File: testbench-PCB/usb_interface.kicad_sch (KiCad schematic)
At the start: 14 parts, among them J1 USB_C_Receptacle_USB2.0, U10 CH340C, U9 USBLC6-2SC6

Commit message: Routing the PCB.
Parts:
- added D1: LED, LED_SMD:LED_0805_2012Metric, symbol Device:LED
- added R4: 500R, Resistor_SMD:R_0805_2012Metric, symbol Device:R
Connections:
- net +5V: now also D1.2 (A)
- net GND: now also R4.2
- new net: D1.1 (K), R4.1
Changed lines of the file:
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@@
+    (stroke (width 0) (type default))
+  )
+  (wire (pts (xy 262.89 118.11) (xy 262.89 121.92))
     (stroke (width 0) (type default))
   )
@@
     (stroke (width 0) (type default))
   )
+  (wire (pts (xy 262.89 105.41) (xy 262.89 110.49))
+    (stroke (width 0) (type default))
+  )
   (wire (pts (xy 218.44 50.8) (xy 218.44 63.5))
     (stroke (width 0) (type default))
@@
   )
   (bus (pts (xy 254 66.04) (xy 254 52.07))
+    (stroke (width 0) (type default))
+  )
+  (wire (pts (xy 262.89 93.98) (xy 262.89 97.79))
     (stroke (width 0) (type default))
   )
@@
         (path "/3ac6901d-218d-4b34-8c4a-bf7c417c33bc/85a3a829-d3a3-466d-ad77-bb3f90e9de82"
           (reference "#PWR06") (unit 1)
+        )
+      )
+    )
+  )
+  (symbol (lib_id "power:GND") (at 262.89 121.92 0) (unit 1)
+    (in_bom yes) (on_board yes) (dnp no) (fields_autoplaced)
+    (property "Reference" "#PWR049" (at 262.89 128.27 0)
+      (effects (font (size 1.27 1.27)) hide)
+    )
+    (property "Value" "GND" (at 262.89 127 0)
+      (effects (font (size 1.27 1.27)))
+    )
+    (property "Footprint" "" (at 262.89 121.92 0)
+      (effects (font (size 1.27 1.27)) hide)
+    )
+    (property "Datasheet" "" (at 262.89 121.92 0)
+      (effects (font (size 1.27 1.27)) hide)
+    )
+    (pin "1")
+    (instances
+      (project "testbench"
+        (path "/3ac6901d-218d-4b34-8c4a-bf7c417c33bc/85a3a829-d3a3-466d-ad77-bb3f90e9de82"
+          (reference "#PWR049") (unit 1)
         )
       )
@@
     )
   )
+  (symbol (lib_id "power:+5V") (at 262.89 93.98 0) (unit 1)
+    (in_bom yes) (on_board yes) (dnp no) (fields_autoplaced)
+    (property "Reference" "#PWR048" (at 262.89 97.79 0)
+      (effects (font (size 1.27 1.27)) hide)
+    )
+    (property "Value" "+5V" (at 262.89 88.9 0)
+      (effects (font (size 1.27 1.27)))
+    )
+    (property "Footprint" "" (at 262.89 93.98 0)
+      (effects (font (size 1.27 1.27)) hide)
+    )
+    (property "Datasheet" "" (at 262.89 93.98 0)
+      (effects (font (size 1.27 1.27)) hide)
+    )
+    (pin "1")
+    (instances
+      (project "testbench"
+        (path "/3ac6901d-218d-4b34-8c4a-bf7c417c33bc/85a3a829-d3a3-466d-ad77-bb3f90e9de82"
+          (reference "#PWR048") (unit 1)
+        )
+      )
+    )
+  )
   (symbol (lib_id "power:GND") (at 111.76 68.58 0) (unit 1)
     (in_bom yes) (on_board yes) (dnp no) (fields_autoplaced)
@@
         (path "/3ac6901d-218d-4b34-8c4a-bf7c417c33bc/85a3a829-d3a3-466d-ad77-bb3f90e9de82"
           (reference "#FLG02") (unit 1)
+        )
+      )
+    )
+  )
+  (symbol (lib_id "Device:R") (at 262.89 114.3 0) (unit 1)
+    (in_bom yes) (on_board yes) (dnp no)
+    (property "Reference" "R4" (at 267.97 114.3 90)
+      (effects (font (size 1.27 1.27)))
+    )
+    (property "Value" "500R" (at 265.43 114.3 90)
+      (effects (font (size 1.27 1.27)))
+    )
+    (property "Footprint" "Resistor_SMD:R_0805_2012Metric" (at 261.112 114.3 90)
+      (effects (font (size 1.27 1.27)) hide)
+    )
+    (property "Datasheet" "~" (at 262.89 114.3 0)
+      (effects (font (size 1.27 1.27)) hide)
+    )
+    (pin "1")
+    (pin "2")
+    (instances
+      (project "testbench"
+        (path "/3ac6901d-218d-4b34-8c4a-bf7c417c33bc"
+          (reference "R4") (unit 1)
+        )
+        (path "/3ac6901d-218d-4b34-8c4a-bf7c417c33bc/08a6730c-9a7c-47f6-b930-4f7799d77218"
+          (reference "R15") (unit 1)
+        )
+        (path "/3ac6901d-218d-4b34-8c4a-bf7c417c33bc/85a3a829-d3a3-466d-ad77-bb3f90e9de82"
+          (reference "R15") (unit 1)
         )
       )
@@
         )
       )
+    )
+  )
+  (symbol (lib_id "Device:LED") (at 262.89 101.6 90) (unit 1)
+    (in_bom yes) (on_board yes) (dnp no)
+    (property "Reference" "D1" (at 259.08 102.87 0)
+      (effects (font (size 1.27 1.27)))
+    )
+    (property "Value" "LED" (at 259.08 103.1875 0)
+      (effects (font (size 1.27 1.27)) hide)
+    )
+    (property "Footprint" "LED_SMD:LED_0805_2012Metric" (at 262.89 101.6 0)
+      (effects (font (size 1.27 1.27)) hide)
+    )
+    (property "Datasheet" "~" (at 262.89 101.6 0)
+      (effects (font (size 1.27 1.27)) hide)
+    )
+    (pin "1")
+    (pin "2")
+    (instances
+      (project "testbench"
+        (path "/3ac6901d-218d-4b34-8c4a-bf7c417c33bc/08a6730c-9a7c-47f6-b930-4f7799d77218"
+          (reference "D1") (unit 1)
+        )
+        (path "/3ac6901d-218d-4b34-8c4a-bf7c417c33bc/85a3a829-d3a3-466d-ad77-bb3f90e9de82"
+          (reference "D1") (unit 1)
+        )
+      )

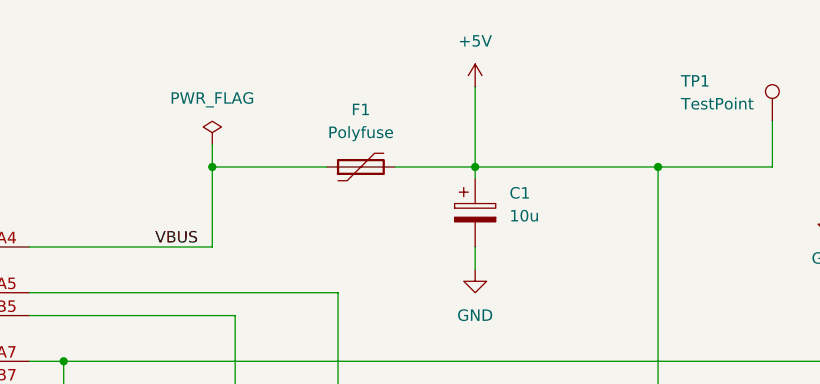
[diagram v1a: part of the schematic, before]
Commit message: Finished PCB routing, added ground plane.
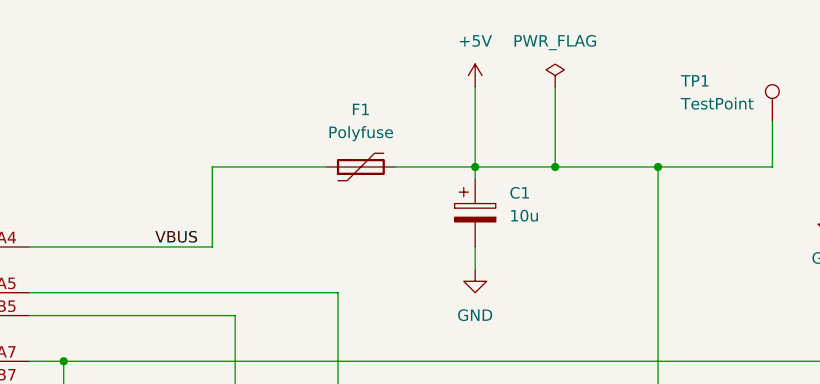
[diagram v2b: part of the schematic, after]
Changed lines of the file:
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@@
   (junction (at 189.23 63.5) (diameter 0) (color 0 0 0 0)
   )
-  (junction (at 82.55 57.15) (diameter 0) (color 0 0 0 0)
-  )
   (junction (at 111.76 57.15) (diameter 0) (color 0 0 0 0)
+  )
+  (junction (at 120.65 57.15) (diameter 0) (color 0 0 0 0)
   )
   (junction (at 66.04 86.36) (diameter 0) (color 0 0 0 0)
@@
     (stroke (width 0) (type default))
   )
-  (wire (pts (xy 82.55 54.61) (xy 82.55 57.15))
-    (stroke (width 0) (type default))
-  )
   (wire (pts (xy 62.23 81.28) (xy 66.04 81.28))
     (stroke (width 0) (type default))
@@
     (stroke (width 0) (type default))
   )
+  (wire (pts (xy 120.65 48.26) (xy 120.65 57.15))
+    (stroke (width 0) (type default))
+  )
   (wire (pts (xy 121.92 106.68) (xy 116.84 106.68))
     (stroke (width 0) (type default))
@@
     (stroke (width 0) (type default))
   )
-  (wire (pts (xy 111.76 57.15) (xy 132.08 57.15))
+  (wire (pts (xy 111.76 57.15) (xy 120.65 57.15))
     (stroke (width 0) (type default))
   )
@@
   )
   (wire (pts (xy 215.9 53.34) (xy 215.9 63.5))
+    (stroke (width 0) (type default))
+  )
+  (wire (pts (xy 120.65 57.15) (xy 132.08 57.15))
     (stroke (width 0) (type default))
   )
@@
         (path "/3ac6901d-218d-4b34-8c4a-bf7c417c33bc/85a3a829-d3a3-466d-ad77-bb3f90e9de82"
           (reference "#PWR05") (unit 1)
+        )
+      )
+    )
+  )
+  (symbol (lib_id "power:PWR_FLAG") (at 120.65 48.26 0) (unit 1)
+    (in_bom yes) (on_board yes) (dnp no) (fields_autoplaced)
+    (property "Reference" "#FLG01" (at 120.65 46.355 0)
+      (effects (font (size 1.27 1.27)) hide)
+    )
+    (property "Value" "PWR_FLAG" (at 120.65 43.18 0)
+      (effects (font (size 1.27 1.27)))
+    )
+    (property "Footprint" "" (at 120.65 48.26 0)
+      (effects (font (size 1.27 1.27)) hide)
+    )
+    (property "Datasheet" "~" (at 120.65 48.26 0)
+      (effects (font (size 1.27 1.27)) hide)
+    )
+    (pin "1")
+    (instances
+      (project "testbench"
+        (path "/3ac6901d-218d-4b34-8c4a-bf7c417c33bc/85a3a829-d3a3-466d-ad77-bb3f90e9de82"
+          (reference "#FLG01") (unit 1)
         )
       )
@@
         )
       )
-    )
-  )
-  (symbol (lib_id "power:PWR_FLAG") (at 82.55 54.61 0) (unit 1)
-    (in_bom yes) (on_board yes) (dnp no) (fields_autoplaced)
-    (property "Reference" "#FLG01" (at 82.55 52.705 0)
-      (effects (font (size 1.27 1.27)) hide)
-    )
-    (property "Value" "PWR_FLAG" (at 82.55 49.53 0)
-      (effects (font (size 1.27 1.27)))
-    )
-    (property "Footprint" "" (at 82.55 54.61 0)
-      (effects (font (size 1.27 1.27)) hide)
-    )
-    (property "Datasheet" "~" (at 82.55 54.61 0)
-      (effects (font (size 1.27 1.27)) hide)
-    )
-    (pin "1")
-    (instances
-      (project "testbench"
-        (path "/3ac6901d-218d-4b34-8c4a-bf7c417c33bc/85a3a829-d3a3-466d-ad77-bb3f90e9de82"
-          (reference "#FLG01") (unit 1)
-        )
-      )

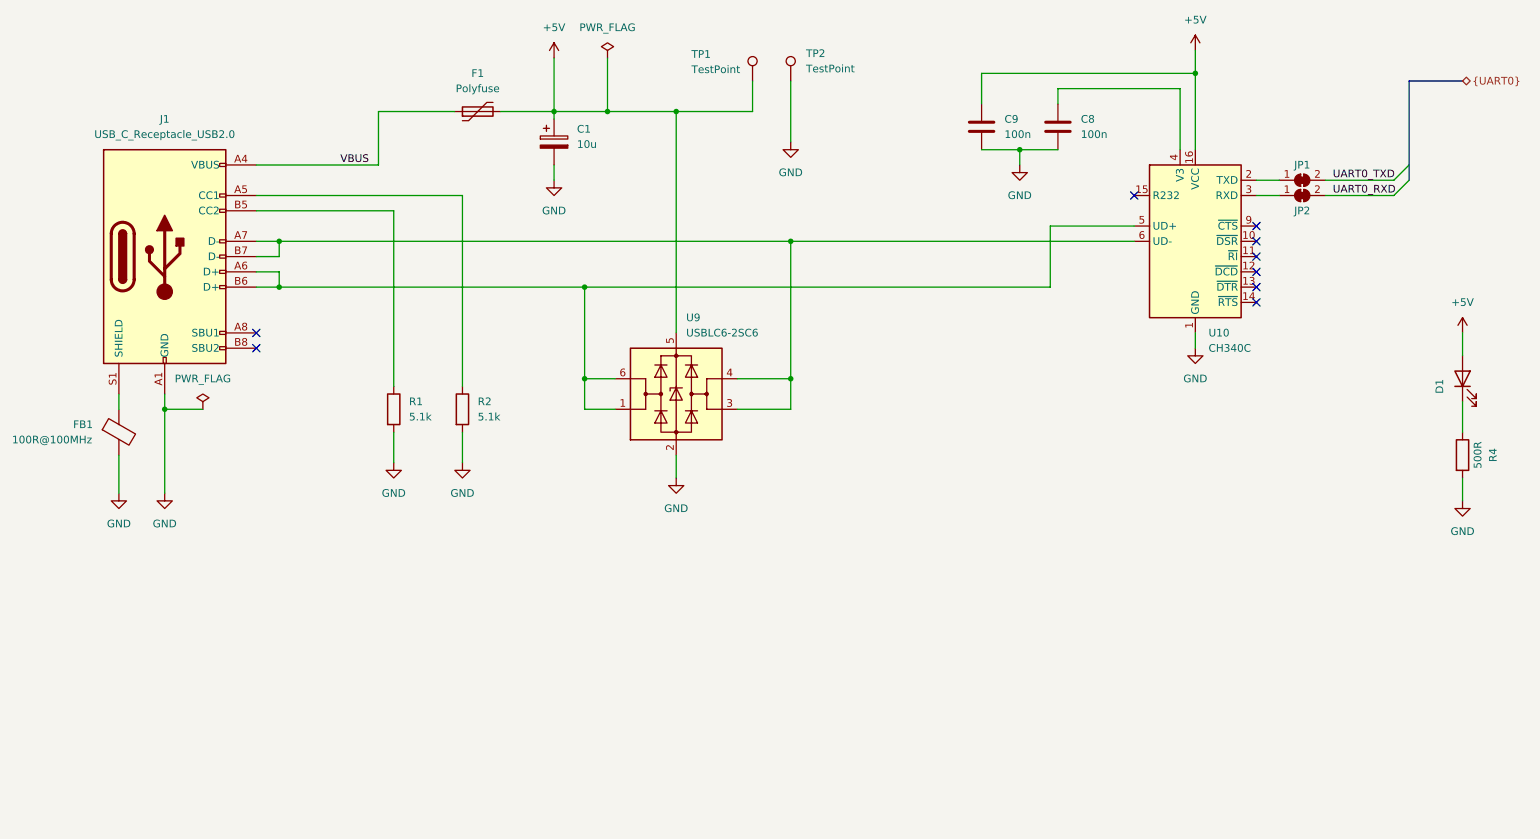
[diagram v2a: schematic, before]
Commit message: Changes regarding part selection.
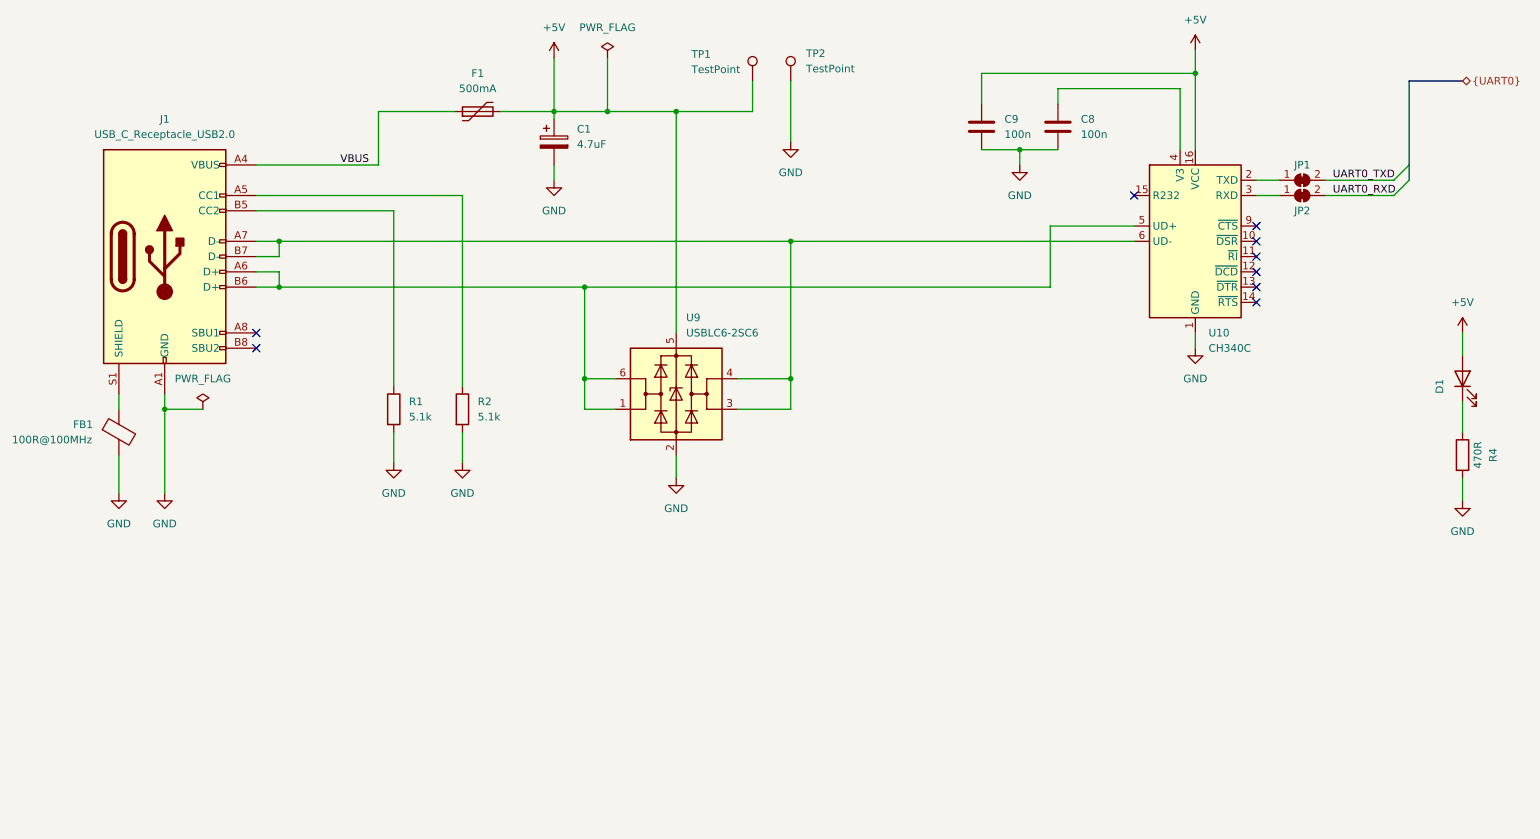
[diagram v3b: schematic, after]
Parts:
- C1: value 10u -> 4.7uF
- F1: value Polyfuse -> 500mA; footprint Fuse:Fuse_1812_4532Metric -> Fuse:Fuse_0805_2012Metric
- R4: value 500R -> 470R
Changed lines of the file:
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@@
       (effects (font (size 1.27 1.27)) (justify left))
     )
-    (property "Value" "10u" (at 115.57 62.611 0)
+    (property "Value" "4.7uF" (at 115.57 62.611 0)
       (effects (font (size 1.27 1.27)) (justify left))
     )
@@
       (effects (font (size 1.27 1.27)))
     )
-    (property "Value" "500R" (at 265.43 114.3 90)
+    (property "Value" "470R" (at 265.43 114.3 90)
       (effects (font (size 1.27 1.27)))
     )
@@
       (effects (font (size 1.27 1.27)))
     )
-    (property "Value" "Polyfuse" (at 99.06 53.34 90)
-      (effects (font (size 1.27 1.27)))
-    )
-    (property "Footprint" "Fuse:Fuse_1812_4532Metric" (at 104.14 55.88 0)
+    (property "Value" "500mA" (at 99.06 53.34 90)
+      (effects (font (size 1.27 1.27)))
+    )
+    (property "Footprint" "Fuse:Fuse_0805_2012Metric" (at 104.14 55.88 0)
       (effects (font (size 1.27 1.27)) (justify left) hide)
     )

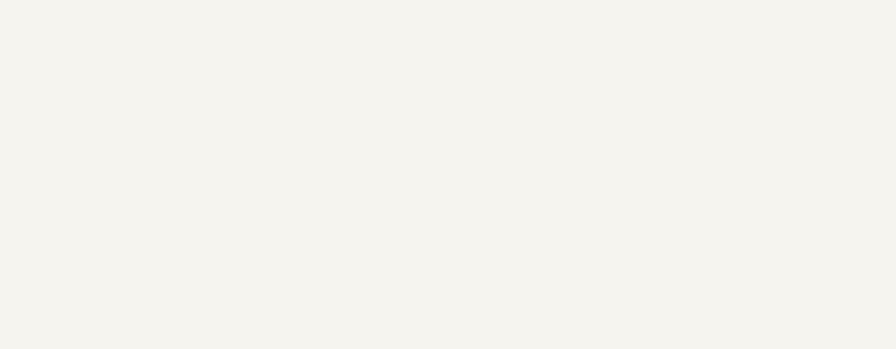
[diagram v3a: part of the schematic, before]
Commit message: Added titles to schematics.
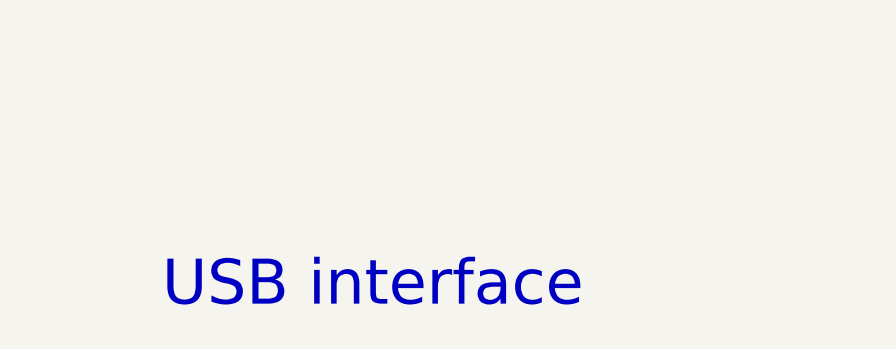
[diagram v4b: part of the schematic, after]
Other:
- note added: "USB interface"
- company: (none) -> Company: VUT Brno
- title: (none) -> Test benches for microcontroller kits
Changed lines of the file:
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@@
 (kicad_sch (version 20230121) (generator eeschema)
   (paper "A4")
+  (title_block
+    (title "Test benches for microcontroller kits")
+    (date "2023")
+    (rev "v0.1")
+    (company "Company: VUT Brno")
+    (comment 1 "Author: Ivo Zaludek")
+  )
   (bus_alias "UART0" (members "UART0_TXD" "UART0_RXD"))
   (junction (at 46.99 106.68) (diameter 0) (color 0 0 0 0)
@@
     (stroke (width 0) (type default))
   )
+  (text "USB interface" (at 179.07 173.99 0)
+    (effects (font (size 5 5)) (justify left bottom))
+  )
   (label "UART0_TXD" (at 241.3 68.58 0) (fields_autoplaced)
